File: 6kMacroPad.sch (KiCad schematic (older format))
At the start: 28 parts, among them J1 USB_mini_micro_B, K1 KEYSW, K2 KEYSW, K3 KEYSW, K4 KEYSW, K5 KEYSW, K6 KEYSW, SW1 SW_PUSH, U1 ATMEGA32U4, Y1 Crystal_GND24

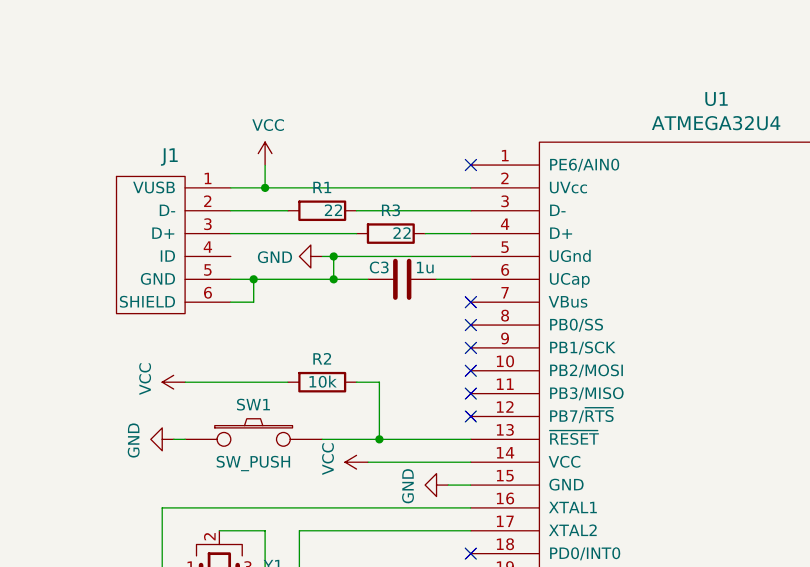
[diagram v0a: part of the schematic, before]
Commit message: Fixed Vbus not connected, added pics
- now Vbus is connected to VCC
- added more pics of the build
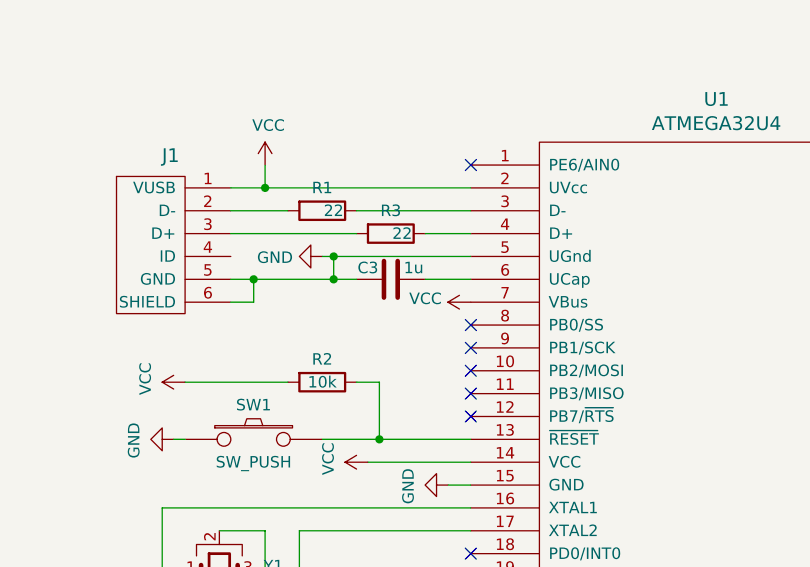
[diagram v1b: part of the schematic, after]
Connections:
- net VCC: now also U1.7 (VBus)
- no-connect marks 23 -> 22
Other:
- moved on the sheet: C3
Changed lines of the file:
@@
 L Device:C C3
 U 1 1 5F2086EA
-P 3100 3050
-F 0 "C3" V 3050 2950 50  0000 C CNN
-F 1 "1u" V 3050 3150 50  0000 C CNN
-F 2 "Capacitor_SMD:C_0805_2012Metric_Pad1.15x1.40mm_HandSolder" H 3138 2900 50  0001 C CNN
-F 3 "~" H 3100 3050 50  0001 C CNN
-	1    3100 3050
+P 3050 3050
+F 0 "C3" V 3000 2950 50  0000 C CNN
+F 1 "1u" V 3000 3150 50  0000 C CNN
+F 2 "Capacitor_SMD:C_0805_2012Metric_Pad1.15x1.40mm_HandSolder" H 3088 2900 50  0001 C CNN
+F 3 "~" H 3050 3050 50  0001 C CNN
+	1    3050 3050
 	0    1    1    0
 $EndComp
 Wire Wire Line
-	3250 3050 3400 3050
-Wire Wire Line
-	2950 3050 2800 3050
+	3200 3050 3400 3050
+Wire Wire Line
+	2900 3050 2800 3050
 Connection ~ 2800 3050
 $Comp
@@
 Wire Wire Line
 	5550 3150 5700 3150
-NoConn ~ 3400 3150
 NoConn ~ 3400 3250
 NoConn ~ 3400 3350
@@
 Wire Wire Line
 	2300 4900 2500 4900
+$Comp
+L power:VCC #PWR?
+U 1 1 5F25B9C4
+P 3400 3150
+F 0 "#PWR?" H 3400 3000 50  0001 C CNN
+F 1 "VCC" V 3415 3277 50  0000 L CNN
+F 2 "" H 3400 3150 50  0001 C CNN
+F 3 "" H 3400 3150 50  0001 C CNN
+	1    3400 3150
+	0    -1   -1   0
+$EndComp
 $EndSCHEMATC
